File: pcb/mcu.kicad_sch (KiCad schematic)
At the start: 9 parts, among them J700 Conn_01x20, J701 BL_CONN, SW700 ON_OFF, U700 xiao-ble, U701 PCA9555PW

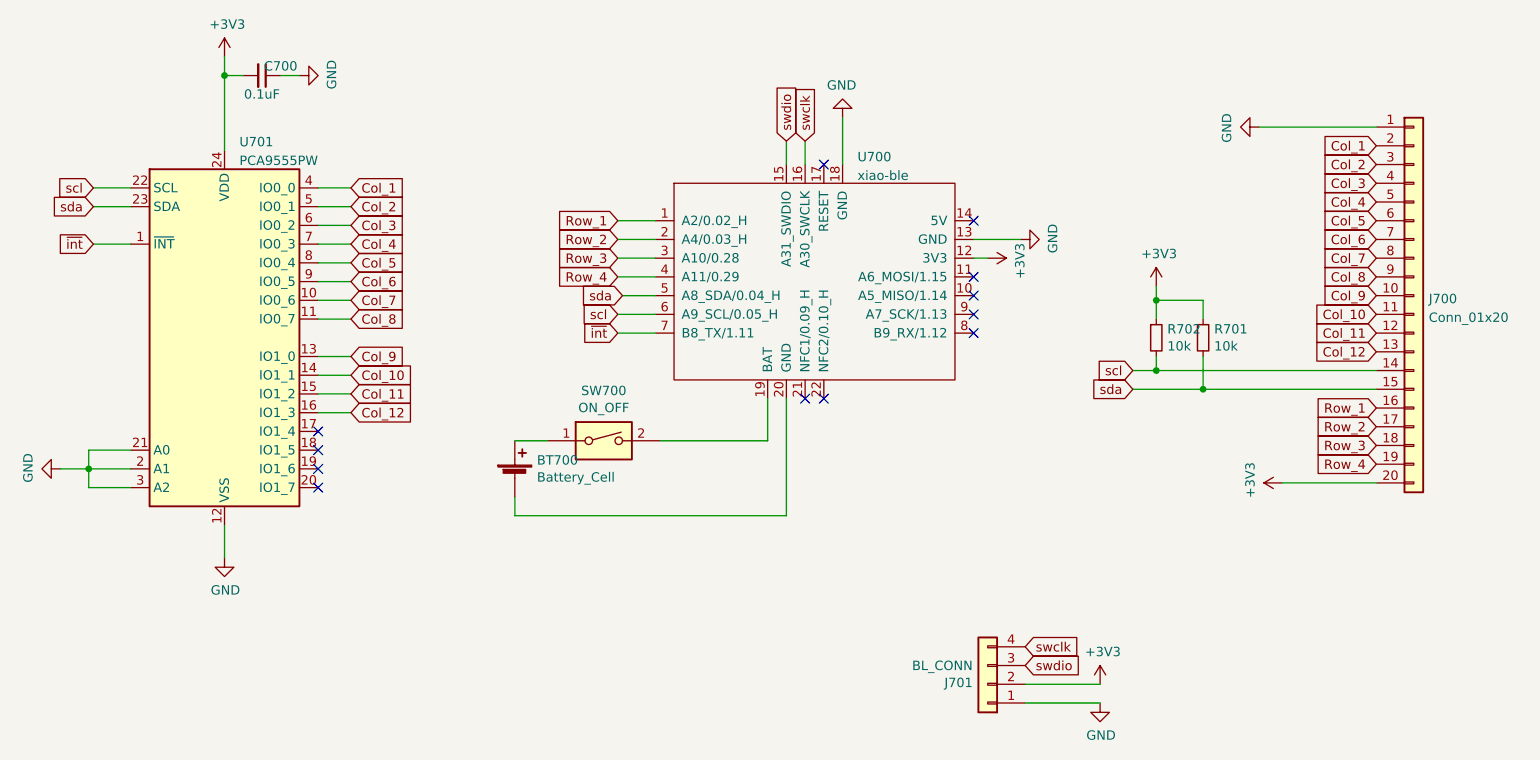
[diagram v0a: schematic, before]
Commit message: Added interrupt lines and GPIO breakout
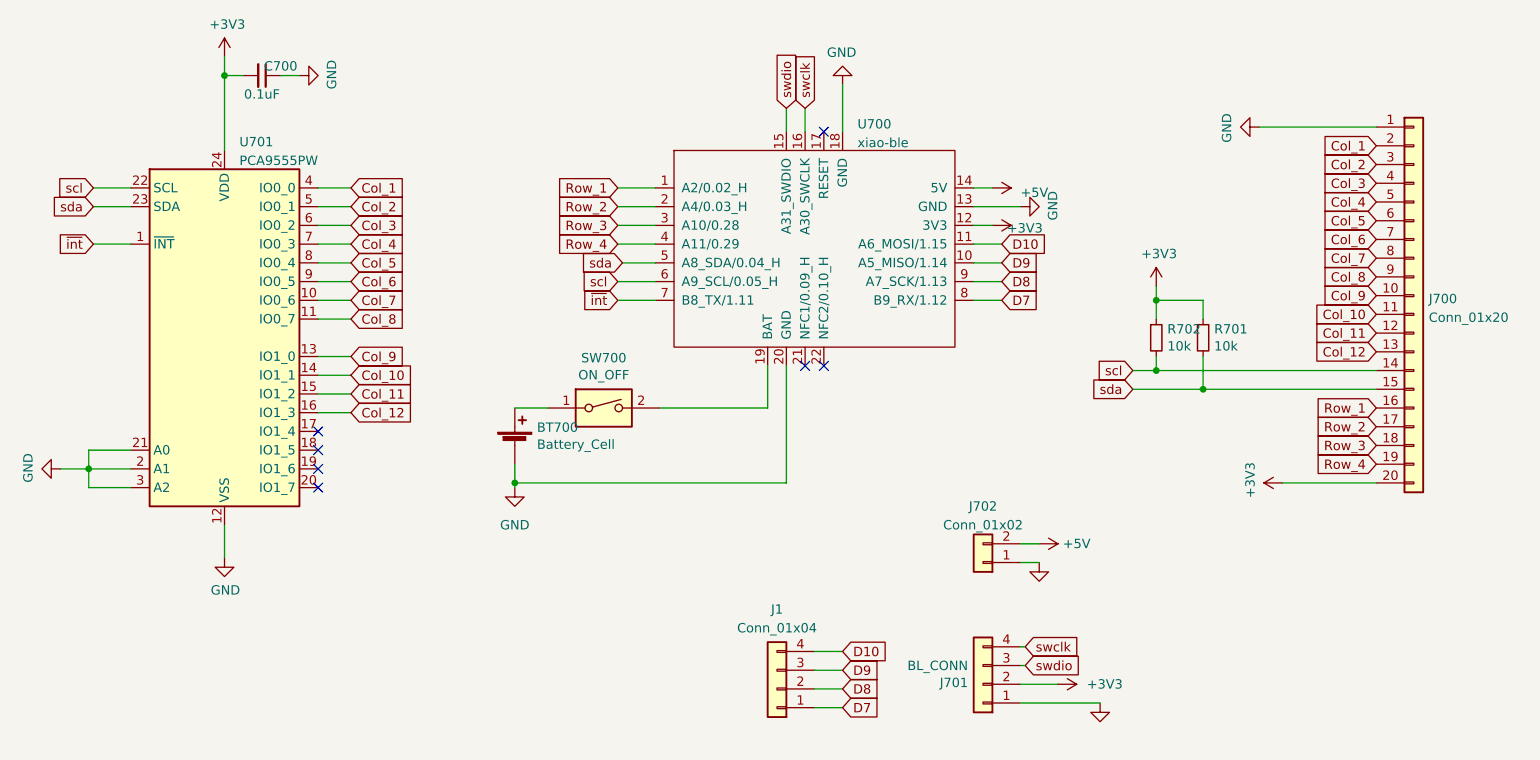
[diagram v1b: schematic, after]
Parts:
- added J1: Conn_01x04, Connector_PinHeader_2.00mm:PinHeader_2x02_P2.00mm_Horizontal, symbol Connector_Generic:Conn_01x04
- added J702: Conn_01x02, Connector_PinHeader_2.54mm:PinHeader_1x02_P2.54mm_Vertical, symbol Connector_Generic:Conn_01x02
- BT700: footprint Connector_Molex:Molex_PicoBlade_53048-0210_1x02_P1.25mm_Horizontal -> Connector_PinHeader_2.00mm:PinHeader_1x02_P2.00mm_Vertical
- R701, R702: footprint Resistor_SMD:R_0805_2012Metric -> Resistor_SMD:R_0805_2012Metric_Pad1.20x1.40mm_HandSolder
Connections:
- net GND: now also BT700.2 (-), U700.20 (GND), J702.1 (Pin_1)
- net D9: now reaches U700.10 (A5_MISO/1.14)
- net D9: now also J1.3 (Pin_3)
- net D10: now reaches U700.11 (A6_MOSI/1.15)
- net D10: now also J1.4 (Pin_4)
- net +5V: now reaches U700.14 (5V)
- net +5V: now also J702.2 (Pin_2)
- net D7: now reaches U700.8 (B9_RX/1.12)
- net D7: now also J1.1 (Pin_1)
- net D8: now reaches U700.9 (A7_SCK/1.13)
- net D8: now also J1.2 (Pin_2)
- no-connect marks 12 -> 7
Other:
- moved on the sheet: BT700, J701, SW700, U700
